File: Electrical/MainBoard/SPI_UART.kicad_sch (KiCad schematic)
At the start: 7 parts, among them J18 Conn_02x02_Odd_Even, J19 Conn_02x03_Odd_Even, J20 Conn_01x06, J22 Conn_02x02_Odd_Even, J23 Conn_02x03_Odd_Even, J27 Conn_01x06_Socket, J8 Conn_02x04_Odd_Even

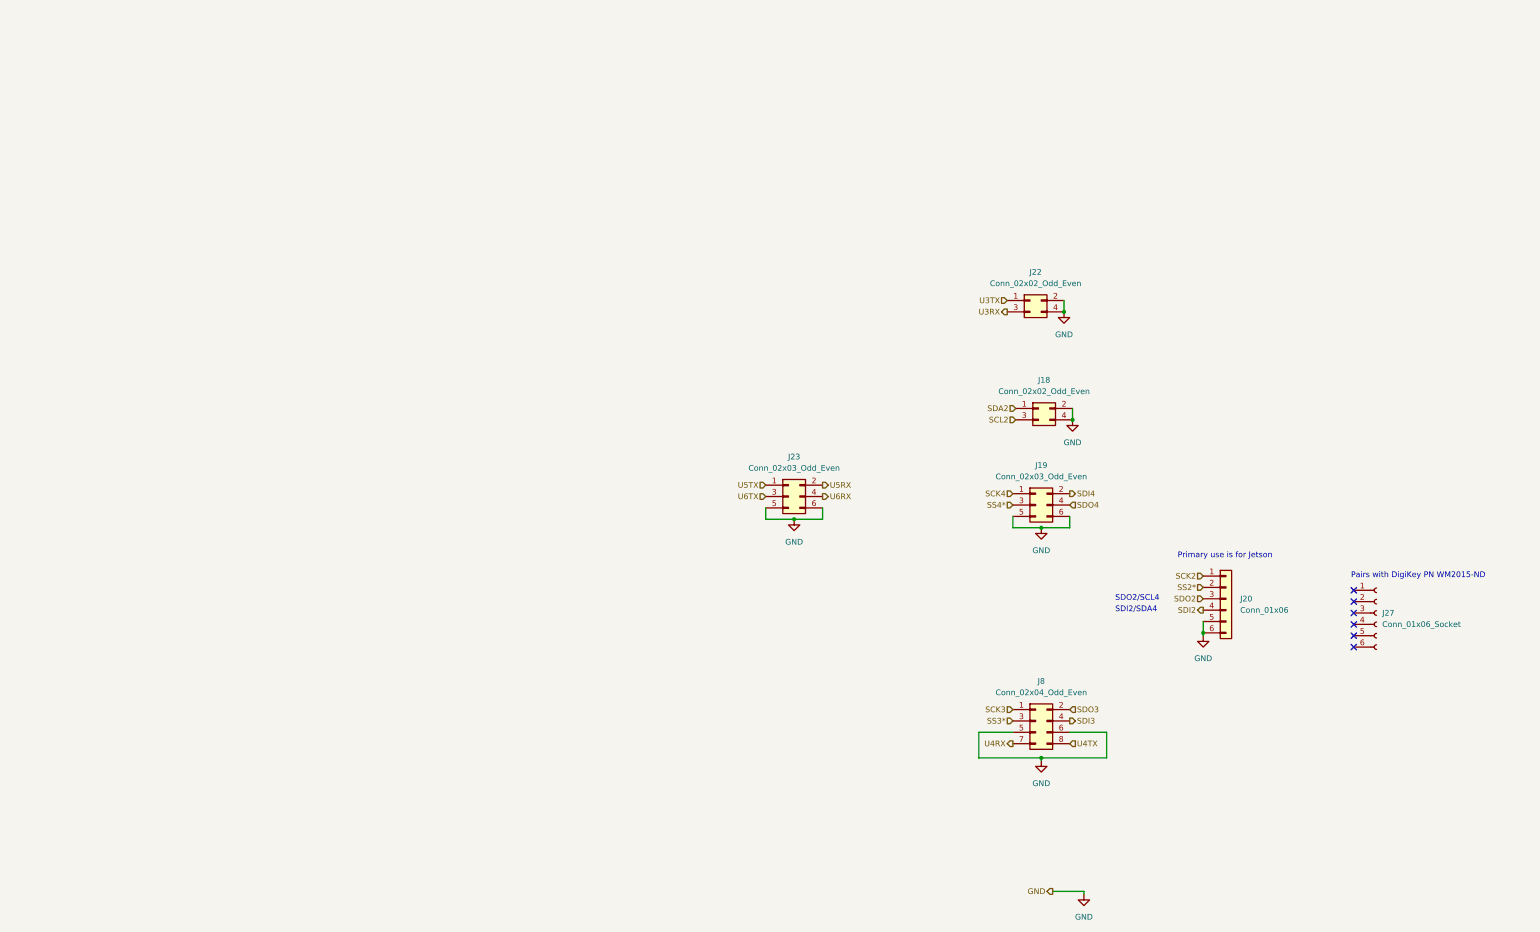
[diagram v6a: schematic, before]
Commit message: Fix SPI3 and make visual improvements
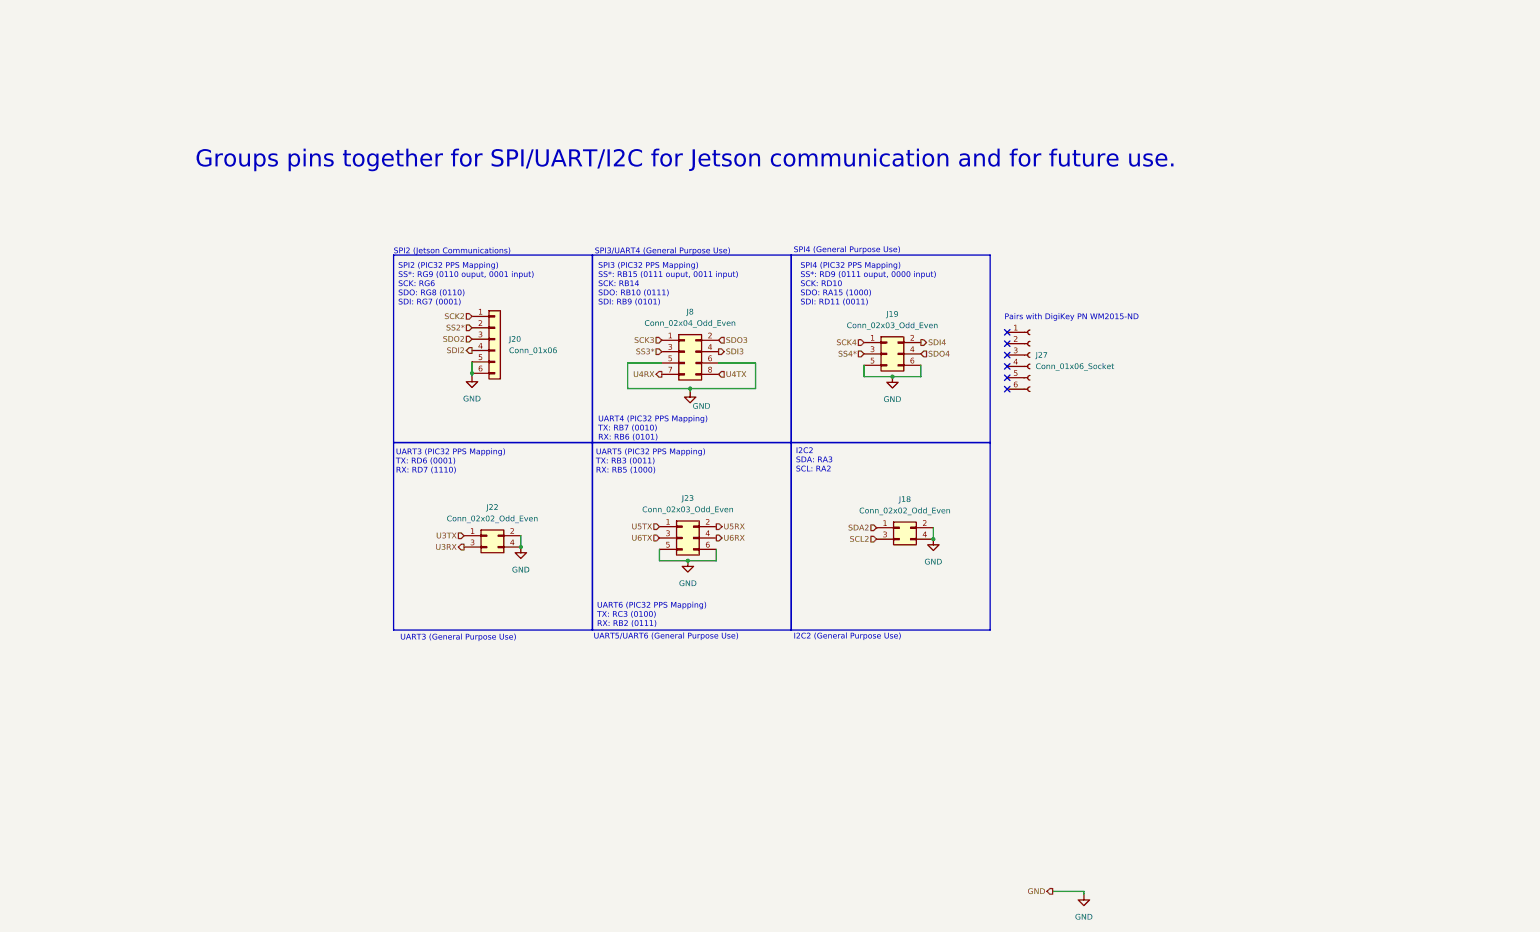
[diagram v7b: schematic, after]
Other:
- note added: "Groups pins together for SPI/UART/I2C for Jetson communication and for future use."
- note added: "I2C2 (General Purpose Use)"
- note added: "I2C2 SDA: RA3 SCL: RA2"
- note added: "SPI2 (Jetson Communications)"
- note added: "SPI2 (PIC32 PPS Mapping) SS*: RG9 (0110 ouput, 0001 input) SCK: RG6 SDO: RG8 (0110) SDI: RG7 (0001)"
- note added: "SPI3 (PIC32 PPS Mapping) SS*: RB15 (0111 ouput, 0011 input) SCK: RB14 SDO: RB10 (0111) SDI: RB9 (0101)"
- note added: "SPI3/UART4 (General Purpose Use)"
- note added: "SPI4 (General Purpose Use)"
- note added: "SPI4 (PIC32 PPS Mapping) SS*: RD9 (0111 ouput, 0000 input) SCK: RD10 SDO: RA15 (1000) SDI: RD11 (0011)"
- note added: "UART3 (General Purpose Use)"
- note added: "UART3 (PIC32 PPS Mapping) TX: RD6 (0001) RX: RD7 (1110)"
- note added: "UART4 (PIC32 PPS Mapping) TX: RB7 (0010) RX: RB6 (0101)"
- note added: "UART5 (PIC32 PPS Mapping) TX: RB3 (0011) RX: RB5 (1000)"
- note added: "UART5/UART6 (General Purpose Use)"
- note added: "UART6 (PIC32 PPS Mapping) TX: RC3 (0100) RX: RB2 (0111)"
- note removed: "Primary use is for Jetson"
- note removed: "SDI2/SDA4"
- note removed: "SDO2/SCL4"
- moved on the sheet: J18, J19, J20, J22, J23, J27, J8

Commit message: Update some parts
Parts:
- J18, J19, J22, J23, J8: now left out of the parts list
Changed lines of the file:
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@@
 		(unit 1)
 		(exclude_from_sim no)
-		(in_bom yes)
+		(in_bom no)
 		(on_board yes)
 		(dnp no)
@@
 		(unit 1)
 		(exclude_from_sim no)
-		(in_bom yes)
+		(in_bom no)
 		(on_board yes)
 		(dnp no)
@@
 		(unit 1)
 		(exclude_from_sim no)
-		(in_bom yes)
+		(in_bom no)
 		(on_board yes)
 		(dnp no)
@@
 		(unit 1)
 		(exclude_from_sim no)
-		(in_bom yes)
+		(in_bom no)
 		(on_board yes)
 		(dnp no)
@@
 		(unit 1)
 		(exclude_from_sim no)
-		(in_bom yes)
+		(in_bom no)
 		(on_board yes)
 		(dnp no)
